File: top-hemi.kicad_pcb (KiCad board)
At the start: 2 copper layers, 46 x 39 mm, 37 parts, among them J1 USB_B_Mini, J2 TC2030_NL, J3 FFC-0.5MM-6POS, J4 Port_1, J5 Port_2, J6 FFC-0.5MM-6POS, J7 Port_3, J8 Port_4, U1 PMIC-LDO-XC6204B332MR_SOT23-5_, U2 LP2985-5.0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

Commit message: Rearrange components
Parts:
- moved J2 11.8 mm to (141.9, 83.4)
- moved mouse-bite-2mm-slot 8.50 mm to (130.5, 83.0)
- moved mouse-bite-2mm-slot 8.49 mm to (163.5, 83.0)
- moved J8 8.34 mm to (167.0, 86.2), turned to 270 degrees
- moved J6 7.38 mm to (142.9, 98.4), turned to 180 degrees
- moved J7 5.66 mm to (127.1, 86.5)
- moved J5 5.65 mm to (166.9, 79.8), turned to 270 degrees
- moved J3 5.10 mm to (152.0, 81.0)
- moved J4 2.51 mm to (127.3, 79.6)
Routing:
- net /Top Hemisphere/BNC-2: track 31.5 -> 0.00 mm, vias 3 -> 0
- net +5V: track 88.9 -> 59.1 mm, vias 8 -> 7
- net /Top Hemisphere/DOUT-BOT: track 20.7 -> 0.08 mm
- net /Top Hemisphere/BATT-BOT: track 22.9 -> 6.12 mm, vias 1 -> 0
- net /Bottom hemisphere/BNC-4: track 13.4 -> 0.00 mm, vias 1 -> 0
- net /Top Hemisphere/MOSI: track 13.1 -> 0.00 mm, vias 2 -> 0
- net /Bottom hemisphere/DIN-BOT: track 8.58 -> 0.00 mm
- net /Top Hemisphere/BNC-4: track 8.39 -> 0.00 mm
- net /Top Hemisphere/MISO: track 12.0 -> 4.19 mm, vias 2 -> 1
- net /Top Hemisphere/BNC-3: track 7.79 -> 0.00 mm, vias 2 -> 0
- net /Top Hemisphere/~RST: track 14.9 -> 8.11 mm, vias 2 -> 0
- net /Bottom hemisphere/BATT-BOT: track 42.5 -> 36.0 mm, vias 1 -> 0
- net GND: track 61.4 -> 56.9 mm, vias 17 -> 10
- net /Top Hemisphere/BNC-1: track 14.0 -> 16.6 mm
- net /Bottom hemisphere/BNC-3: track 25.5 -> 23.4 mm

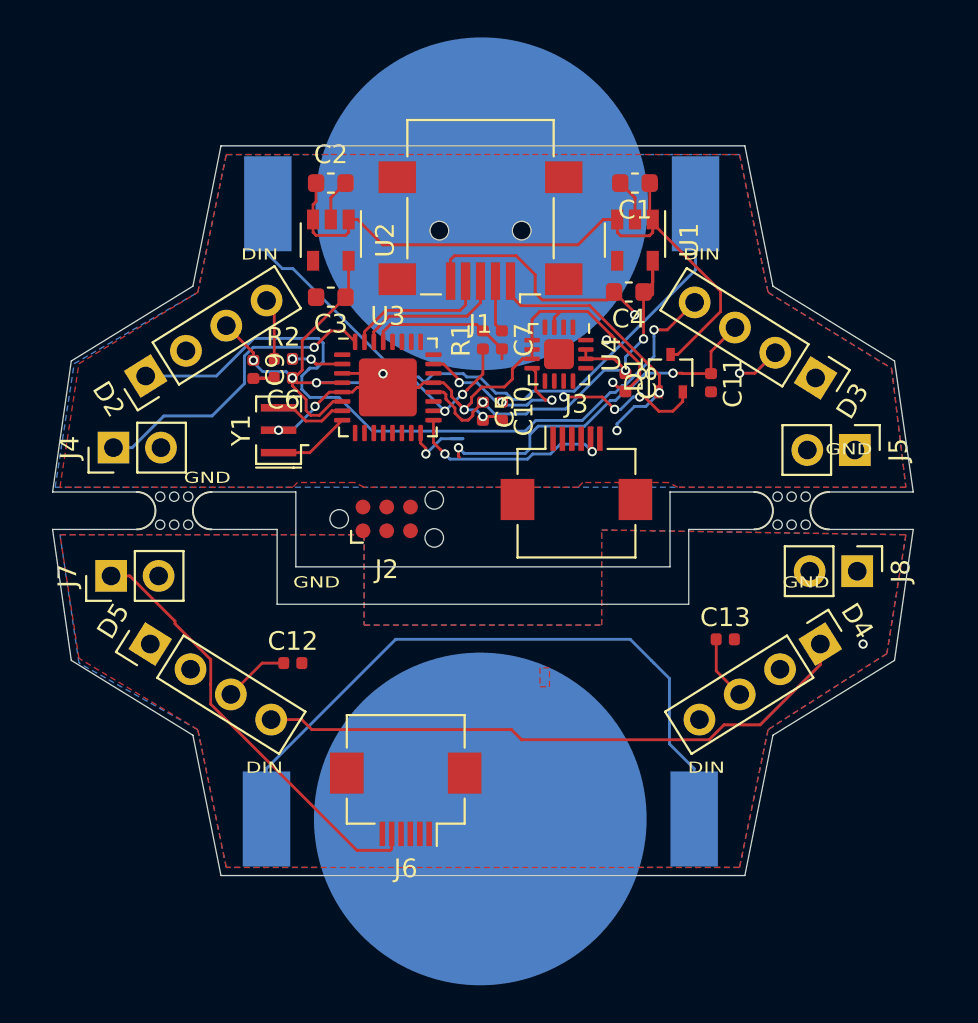
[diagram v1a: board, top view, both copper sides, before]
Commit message: Route bottom board
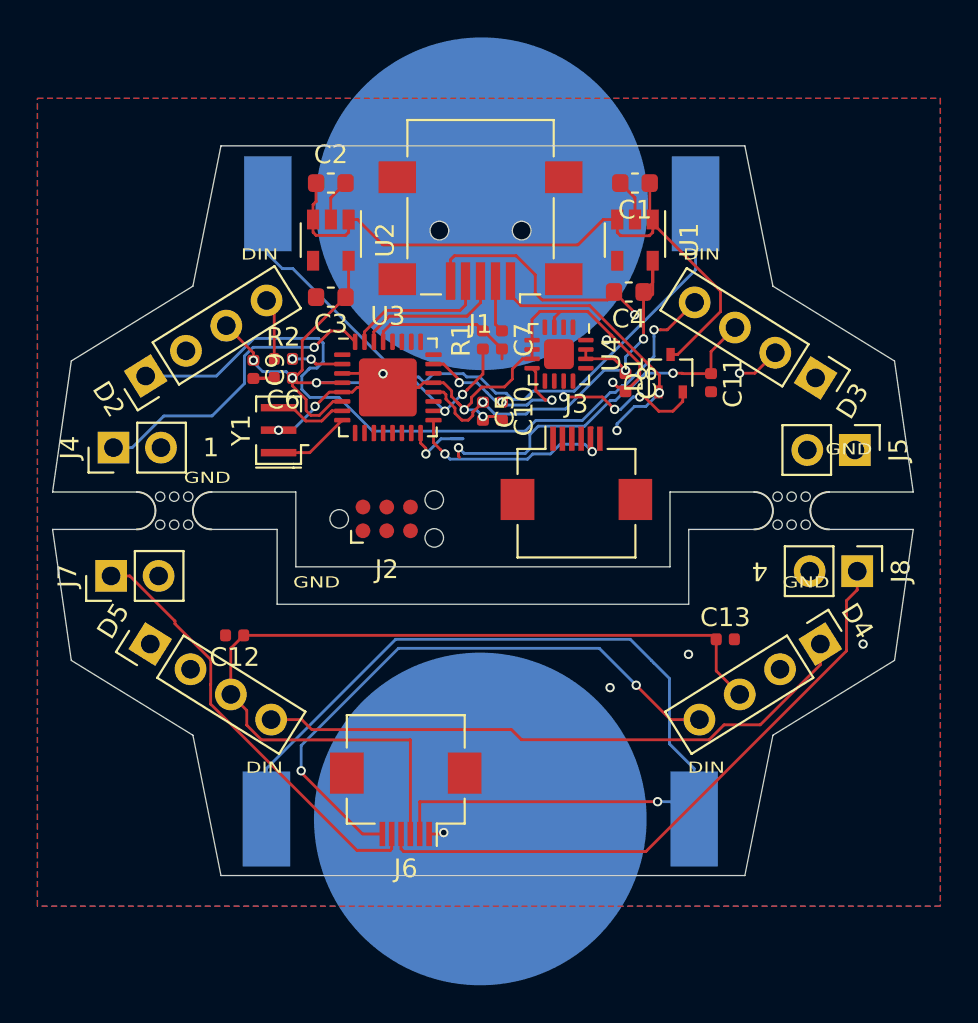
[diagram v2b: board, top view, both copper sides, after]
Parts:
- moved C12 3.44 mm to (133.7, 89.7), turned to 180 degrees
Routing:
- net +5V: track 59.1 -> 100.4 mm
- net /Bottom hemisphere/BNC-4: track 0.00 -> 33.6 mm
- net /Bottom hemisphere/DIN-BOT: track 0.00 -> 32.2 mm, vias 0 -> 2
- net /Bottom hemisphere/BATT-BOT: track 36.0 -> 52.8 mm, vias 0 -> 1
- net GND: track 56.9 -> 57.7 mm, vias 10 -> 13
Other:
- board text added: "1"
- board text added: "2"
- board text added: "3"
- board text added: "4"

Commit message: Route some more at the top
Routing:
- net /Top Hemisphere/~RST: track 8.11 -> 32.0 mm, vias 0 -> 2
- net +5V: track 100.4 -> 84.0 mm, vias 7 -> 5
- net /Top Hemisphere/+5V_EXT: track 14.7 -> 27.6 mm
- net /Top Hemisphere/MOSI: track 0.00 -> 8.62 mm
- net /Top Hemisphere/SCK: track 10.5 -> 6.95 mm, vias 2 -> 0
- net /Top Hemisphere/MISO: track 4.19 -> 4.70 mm, vias 1 -> 0

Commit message: Reduce pour clearance to 10mils (>= 8mils specs)
Seeed specs:

http://support.seeedstudio.com/knowledgebase/articles/447362-fusion-pcb-specification
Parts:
- D2: value NeoPixel_THT -> LED 1
- D3: value NeoPixel_THT -> LED 2
- D4: value NeoPixel_THT -> LED 3
- D5: value NeoPixel_THT -> LED 4
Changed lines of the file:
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@@
     (user_trace_width 0.1524)
     (trace_clearance 0.1524)
-    (zone_clearance 0.508)
+    (zone_clearance 0.254)
     (zone_45_only no)
     (trace_min 0.1016)
@@
       (effects (font (size 1 1) (thickness 0.15)))
     )
-    (fp_text value NeoPixel_THT (at 0 9.95 122) (layer F.Fab)
+    (fp_text value "LED 1" (at 0 9.95 122) (layer F.Fab)
       (effects (font (size 1 1) (thickness 0.15)))
     )
@@
       (effects (font (size 1 1) (thickness 0.15)))
     )
-    (fp_text value NeoPixel_THT (at 0 9.95 238) (layer F.Fab)
+    (fp_text value "LED 2" (at 0 9.95 238) (layer F.Fab)
       (effects (font (size 1 1) (thickness 0.15)))
     )
@@
       (effects (font (size 1 1) (thickness 0.15)))
     )
-    (fp_text value NeoPixel_THT (at 0 9.95 302) (layer F.Fab)
+    (fp_text value "LED 3" (at 0 9.95 302) (layer F.Fab)
       (effects (font (size 1 1) (thickness 0.15)))
     )
@@
       (effects (font (size 1 1) (thickness 0.15)))
     )
-    (fp_text value NeoPixel_THT (at 0 9.95 58) (layer F.Fab)
+    (fp_text value "LED 4" (at 0 9.95 58) (layer F.Fab)
       (effects (font (size 1 1) (thickness 0.15)))
     )
@@
   (segment (start 135.847 72.172963) (end 135.438042 71.764005) (width 0.1524) (layer F.Cu) (net 13) (status 30))
   (segment (start 135.847 74.888) (end 135.847 72.172963) (width 0.1524) (layer F.Cu) (net 13) (status 30))
+  (segment (start 152.842 78.571) (end 152.759928 78.571) (width 0.1524) (layer F.Cu) (net 14))
   (segment (start 161.818301 94.446) (end 165.034 91.230301) (width 0.1524) (layer F.Cu) (net 15))
   (segment (start 159.888189 94.446) (end 161.818301 94.446) (width 0.1524) (layer F.Cu) (net 15))
@@
   (segment (start 149.068586 95.244586) (end 159.089603 95.244586) (width 0.1524) (layer F.Cu) (net 15))
   (segment (start 159.089603 95.244586) (end 159.888189 94.446) (width 0.1524) (layer F.Cu) (net 15))
-  (segment (start 146.873 71.8824) (end 146.873 70.73) (width 0.1524) (layer F.Cu) (net 17) (status 20))
-  (segment (start 146.1534 72.602) (end 146.873 71.8824) (width 0.1524) (layer F.Cu) (net 17))
-  (segment (start 142.005 72.602) (end 146.1534 72.602) (width 0.1524) (layer F.Cu) (net 17))
-  (segment (start 141.17 73.437) (end 142.005 72.602) (width 0.1524) (layer F.Cu) (net 17))
-  (segment (start 141.17 73.9745) (end 141.17 73.437) (width 0.1524) (layer F.Cu) (net 17) (status 10))
-  (segment (start 140.67 73.437) (end 140.67 73.9745) (width 0.1524) (layer F.Cu) (net 18) (status 20))
-  (segment (start 141.809809 72.297191) (end 140.67 73.437) (width 0.1524) (layer F.Cu) (net 18))
-  (segment (start 145.78081 72.29719) (end 141.809809 72.297191) (width 0.1524) (layer F.Cu) (net 18))
-  (segment (start 146.073 72.005) (end 145.78081 72.29719) (width 0.1524) (layer F.Cu) (net 18))
-  (segment (start 146.073 70.73) (end 146.073 72.005) (width 0.1524) (layer F.Cu) (net 18) (status 10))
-  (segment (start 152.842 78.571) (end 152.759928 78.571) (width 0.1524) (layer F.Cu) (net 14))
   (via (at 137.287 96.901) (size 0.5) (drill 0.3) (layers F.Cu B.Cu) (net 16))
   (segment (start 137.287 96.998482) (end 137.287 96.901) (width 0.1524) (layer F.Cu) (net 16))
@@
   (segment (start 157.030985 94.165985) (end 158.571874 94.165985) (width 0.1524) (layer F.Cu) (net 16))
   (segment (start 155.194 92.329) (end 157.030985 94.165985) (width 0.1524) (layer F.Cu) (net 16))
+  (segment (start 146.873 71.8824) (end 146.873 70.73) (width 0.1524) (layer F.Cu) (net 17) (status 20))
+  (segment (start 146.1534 72.602) (end 146.873 71.8824) (width 0.1524) (layer F.Cu) (net 17))
+  (segment (start 142.005 72.602) (end 146.1534 72.602) (width 0.1524) (layer F.Cu) (net 17))
+  (segment (start 141.17 73.437) (end 142.005 72.602) (width 0.1524) (layer F.Cu) (net 17))
+  (segment (start 141.17 73.9745) (end 141.17 73.437) (width 0.1524) (layer F.Cu) (net 17) (status 10))
+  (segment (start 140.67 73.437) (end 140.67 73.9745) (width 0.1524) (layer F.Cu) (net 18) (status 20))
+  (segment (start 141.809809 72.297191) (end 140.67 73.437) (width 0.1524) (layer F.Cu) (net 18))
+  (segment (start 145.78081 72.29719) (end 141.809809 72.297191) (width 0.1524) (layer F.Cu) (net 18))
+  (segment (start 146.073 72.005) (end 145.78081 72.29719) (width 0.1524) (layer F.Cu) (net 18))
+  (segment (start 146.073 70.73) (end 146.073 72.005) (width 0.1524) (layer F.Cu) (net 18) (status 10))
   (segment (start 141.534897 84.696301) (end 141.236699 84.398103) (width 0.1524) (layer F.Cu) (net 19))
   (segment (start 143.129 84.074) (end 142.506699 84.696301) (width 0.1524) (layer F.Cu) (net 19))
@@
   (segment (start 139.4825 78.162) (end 137.7465 79.898) (width 0.1524) (layer F.Cu) (net 32))
   (zone (net 3) (net_name GND) (layer F.Cu) (hatch edge 0.508)
-    (connect_pads (clearance 0.508))
+    (connect_pads (clearance 0.254))
     (min_thickness 0.254)
     (fill yes (arc_segments 32) (thermal_gap 0.508) (thermal_bridge_width 0.508))
@@
   )
   (zone (net 3) (net_name GND) (layer B.Cu) (hatch edge 0.508)
-    (connect_pads (clearance 0.508))
+    (connect_pads (clearance 0.254))
     (min_thickness 0.254)
     (fill yes (arc_segments 32) (thermal_gap 0.508) (thermal_bridge_width 0.508))

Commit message: Finish routing top board
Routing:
- net /Top Hemisphere/BNC-2: track 0.00 -> 53.5 mm, vias 0 -> 4
- net +5V: track 84.0 -> 101.7 mm, vias 5 -> 9
- net /Top Hemisphere/BNC-4: track 0.00 -> 16.7 mm, vias 0 -> 2
- net /Top Hemisphere/BNC-3: track 0.00 -> 15.7 mm, vias 0 -> 2
- net /Top Hemisphere/BATT-BOT: track 6.12 -> 20.5 mm, vias 0 -> 1
- net /Top Hemisphere/DOUT-BOT: track 0.08 -> 13.9 mm, vias 0 -> 1
- net GND: track 57.7 -> 58.5 mm, vias 13 -> 14

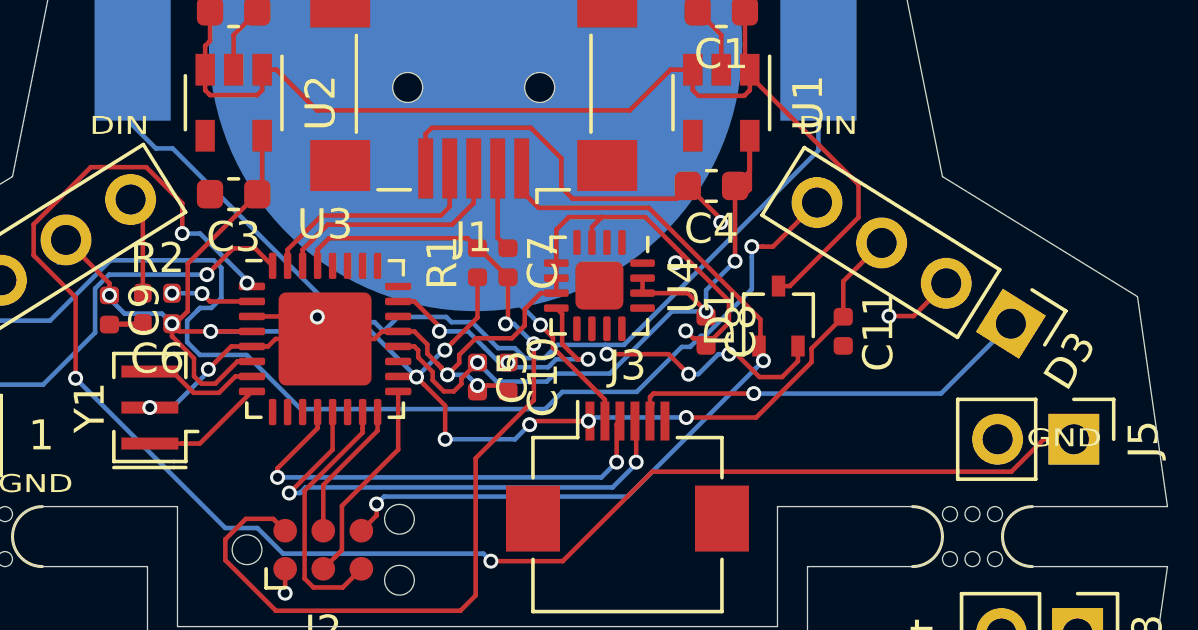
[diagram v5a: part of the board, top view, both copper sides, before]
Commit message: Fix airwires, tighten GND zones (within specs)
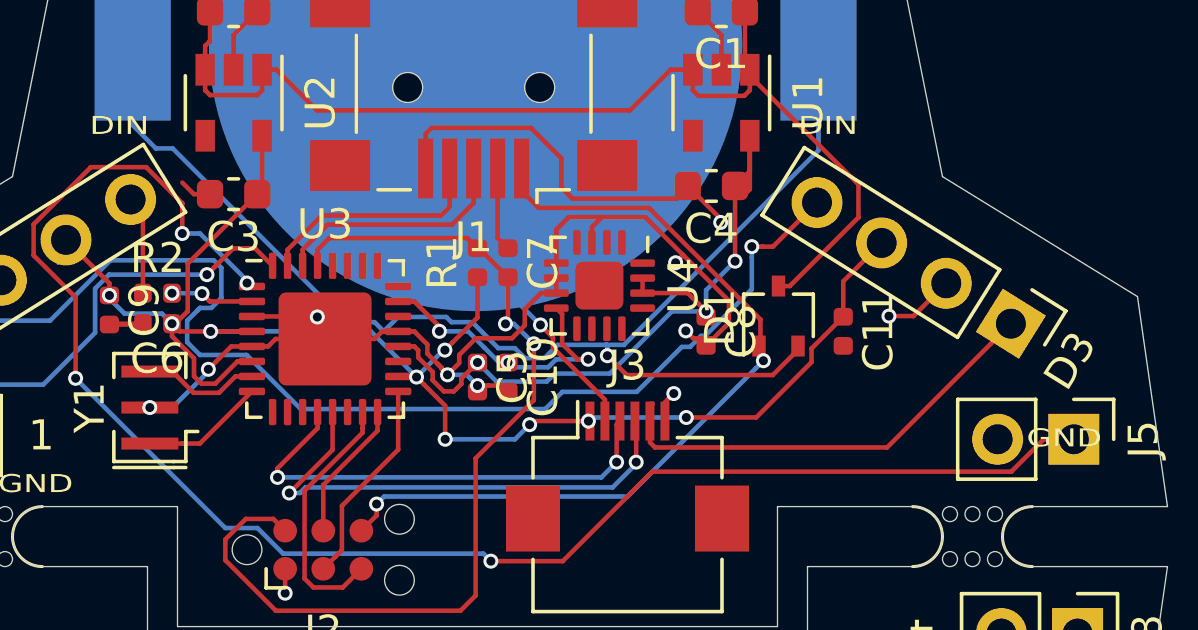
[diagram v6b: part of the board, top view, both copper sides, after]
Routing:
- net GND: track 58.5 -> 60.7 mm, vias 14 -> 15
- net /Top Hemisphere/BATT: track 43.9 -> 43.1 mm, vias 3 -> 1
- net /Top Hemisphere/DOUT-BOT: track 13.9 -> 14.6 mm
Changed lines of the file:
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@@
     (thickness 1)
     (drawings 121)
-    (tracks 504)
+    (tracks 500)
     (zones 0)
     (modules 37)
@@
   (layers
     (0 F.Cu signal)
-    (31 B.Cu signal hide)
+    (31 B.Cu signal)
     (32 B.Adhes user hide)
     (33 F.Adhes user hide)
@@
     (user_trace_width 0.1524)
     (trace_clearance 0.1524)
-    (zone_clearance 0.254)
+    (zone_clearance 0.2032)
     (zone_45_only no)
     (trace_min 0.1016)
@@
   )
   (segment (start 157.683 76.521953) (end 157.698104 76.537057) (width 0.1524) (layer F.Cu) (net 1) (status 30))
-  (segment (start 157.1534 77.682) (end 156.397999 77.682) (width 0.1524) (layer F.Cu) (net 1))
-  (segment (start 157.683 77.1524) (end 157.1534 77.682) (width 0.1524) (layer F.Cu) (net 1))
-  (segment (start 157.683 76.65) (end 157.683 77.1524) (width 0.1524) (layer F.Cu) (net 1))
-  (segment (start 156.397999 77.682) (end 155.636 76.920001) (width 0.1524) (layer F.Cu) (net 1))
-  (via (at 155.382 76.92) (size 0.5) (drill 0.3) (layers F.Cu B.Cu) (net 1))
-  (segment (start 155.382001 76.920001) (end 155.382 76.92) (width 0.1524) (layer F.Cu) (net 1))
-  (segment (start 155.636 76.920001) (end 155.382001 76.920001) (width 0.1524) (layer F.Cu) (net 1))
-  (via (at 151.318 76.92) (size 0.5) (drill 0.3) (layers F.Cu B.Cu) (net 1))
   (segment (start 158.3665 70.1255) (end 158.3665 69.2873) (width 0.1524) (layer B.Cu) (net 1))
   (segment (start 151.881545 76.610455) (end 158.3665 70.1255) (width 0.1524) (layer B.Cu) (net 1))
   (segment (start 158.3665 69.2873) (end 158.3665 66.5949) (width 0.1524) (layer B.Cu) (net 1))
-  (segment (start 151.318 76.666) (end 151.262455 76.610455) (width 0.1524) (layer B.Cu) (net 1))
-  (segment (start 151.318 76.92) (end 151.318 76.666) (width 0.1524) (layer B.Cu) (net 1))
   (segment (start 151.262455 76.610455) (end 151.881545 76.610455) (width 0.1524) (layer B.Cu) (net 1))
   (segment (start 146.133519 75.853189) (end 146.825792 75.853189) (width 0.1524) (layer B.Cu) (net 1))
@@
   (segment (start 143.875067 76.158) (end 144.353668 75.679399) (width 0.1524) (layer B.Cu) (net 1))
   (segment (start 136.84 70.062) (end 142.631189 75.853189) (width 0.1524) (layer B.Cu) (net 1))
-  (segment (start 151.318 76.92) (end 153.372959 76.92) (width 0.1524) (layer F.Cu) (net 1))
-  (segment (start 153.372959 76.92) (end 153.789052 77.336093) (width 0.1524) (layer F.Cu) (net 1))
-  (segment (start 154.362355 77.586092) (end 154.039051 77.586092) (width 0.1524) (layer B.Cu) (net 1))
-  (via (at 154.039051 77.586092) (size 0.5) (drill 0.3) (layers F.Cu B.Cu) (net 1))
-  (segment (start 153.789052 77.336093) (end 154.039051 77.586092) (width 0.1524) (layer F.Cu) (net 1))
-  (segment (start 155.382 76.92) (end 155.028447 76.92) (width 0.1524) (layer B.Cu) (net 1))
-  (segment (start 155.028447 76.92) (end 154.362355 77.586092) (width 0.1524) (layer B.Cu) (net 1))
+  (via (at 151.32942 76.970535) (size 0.5) (drill 0.3) (layers F.Cu B.Cu) (net 1))
+  (segment (start 151.974765 77.61588) (end 151.32942 76.970535) (width 0.1524) (layer F.Cu) (net 1))
+  (segment (start 156.84212 77.61588) (end 151.974765 77.61588) (width 0.1524) (layer F.Cu) (net 1))
+  (segment (start 157.683 76.65) (end 157.683 76.775) (width 0.1524) (layer F.Cu) (net 1))
+  (segment (start 157.683 76.775) (end 156.84212 77.61588) (width 0.1524) (layer F.Cu) (net 1))
+  (segment (start 151.322893 76.610455) (end 151.262455 76.610455) (width 0.1524) (layer B.Cu) (net 1))
+  (segment (start 151.32942 76.616982) (end 151.322893 76.610455) (width 0.1524) (layer B.Cu) (net 1))
+  (segment (start 151.32942 76.970535) (end 151.32942 76.616982) (width 0.1524) (layer B.Cu) (net 1))
   (segment (start 147.308055 66.484579) (end 146.954502 66.484579) (width 0.1524) (layer B.Cu) (net 2) (status 30))
   (segment (start 153.074579 66.484579) (end 147.308055 66.484579) (width 0.1524) (layer B.Cu) (net 2) (status 30))
@@
   (via (at 140.589 84.8868) (size 0.5) (drill 0.3) (layers F.Cu B.Cu) (net 3))
   (segment (start 140.589 84.074) (end 140.589 84.8868) (width 0.1524) (layer F.Cu) (net 3))
+  (via (at 153.543 78.232) (size 0.5) (drill 0.3) (layers F.Cu B.Cu) (net 3))
+  (segment (start 153.25 79.15) (end 153.25 78.525) (width 0.1524) (layer F.Cu) (net 3))
+  (segment (start 153.25 78.525) (end 153.543 78.232) (width 0.1524) (layer F.Cu) (net 3))
+  (segment (start 137.547 71.586) (end 137.16 71.199) (width 0.1524) (layer F.Cu) (net 3))
+  (segment (start 138.0845 71.586) (end 137.547 71.586) (width 0.1524) (layer F.Cu) (net 3))
   (segment (start 156.144 91.144) (end 156.017 91.017) (width 0.1524) (layer B.Cu) (net 4))
   (segment (start 158.2903 96.7828) (end 158.2903 99.4752) (width 0.1524) (layer B.Cu) (net 4) (status 20))
@@
   (segment (start 135.847 74.888) (end 135.847 72.172963) (width 0.1524) (layer F.Cu) (net 13) (status 30))
   (segment (start 152.842 78.571) (end 152.759928 78.571) (width 0.1524) (layer F.Cu) (net 14))
-  (via (at 156.21 78.232) (size 0.5) (drill 0.3) (layers F.Cu B.Cu) (net 14))
-  (segment (start 152.8656 78.232) (end 156.21 78.232) (width 0.1524) (layer F.Cu) (net 14))
-  (segment (start 152.75 79.15) (end 152.75 78.3476) (width 0.1524) (layer F.Cu) (net 14))
-  (segment (start 152.75 78.3476) (end 152.8656 78.232) (width 0.1524) (layer F.Cu) (net 14))
-  (segment (start 162.452 78.232) (end 164.78 75.904) (width 0.1524) (layer B.Cu) (net 14))
-  (segment (start 156.21 78.232) (end 162.452 78.232) (width 0.1524) (layer B.Cu) (net 14))
+  (via (at 164.78 75.904) (size 0.5) (drill 0.3) (layers F.Cu B.Cu) (net 14))
+  (segment (start 164.09244 76.59156) (end 164.78 75.904) (width 0.1524) (layer F.Cu) (net 14))
+  (segment (start 160.655399 80.028601) (end 164.09244 76.59156) (width 0.1524) (layer F.Cu) (net 14))
+  (segment (start 152.917119 80.028601) (end 160.655399 80.028601) (width 0.1524) (layer F.Cu) (net 14))
+  (segment (start 152.75 79.861482) (end 152.917119 80.028601) (width 0.1524) (layer F.Cu) (net 14))
+  (segment (start 152.75 79.15) (end 152.75 79.861482) (width 0.1524) (layer F.Cu) (net 14))
   (segment (start 161.818301 94.446) (end 165.034 91.230301) (width 0.1524) (layer F.Cu) (net 15))
   (segment (start 159.888189 94.446) (end 161.818301 94.446) (width 0.1524) (layer F.Cu) (net 15))
@@
   (segment (start 139.4825 78.162) (end 137.7465 79.898) (width 0.1524) (layer F.Cu) (net 32))
   (zone (net 3) (net_name GND) (layer F.Cu) (hatch edge 0.508)
-    (connect_pads (clearance 0.254))
+    (connect_pads (clearance 0.2032))
     (min_thickness 0.254)
     (fill yes (arc_segments 32) (thermal_gap 0.508) (thermal_bridge_width 0.508))
@@
   )
   (zone (net 3) (net_name GND) (layer B.Cu) (hatch edge 0.508)
-    (connect_pads (clearance 0.254))
+    (connect_pads (clearance 0.2032))
     (min_thickness 0.254)
     (fill yes (arc_segments 32) (thermal_gap 0.508) (thermal_bridge_width 0.508))
